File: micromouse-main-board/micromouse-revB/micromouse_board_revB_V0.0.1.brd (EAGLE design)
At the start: 128.4 x 85.5 mm, 110 parts, among them IC1 LM321MFX, J3 HTSS-103-XX-XX-D, J5 HTSS-103-XX-XX-D, J6 HTSS-102-XX-XX-D, U2 DRV8848PWPR, U3 ACS712ELCTR-20A-T, U6 MPU-6000, X1 RASPI_GPIO_B+#_PIN

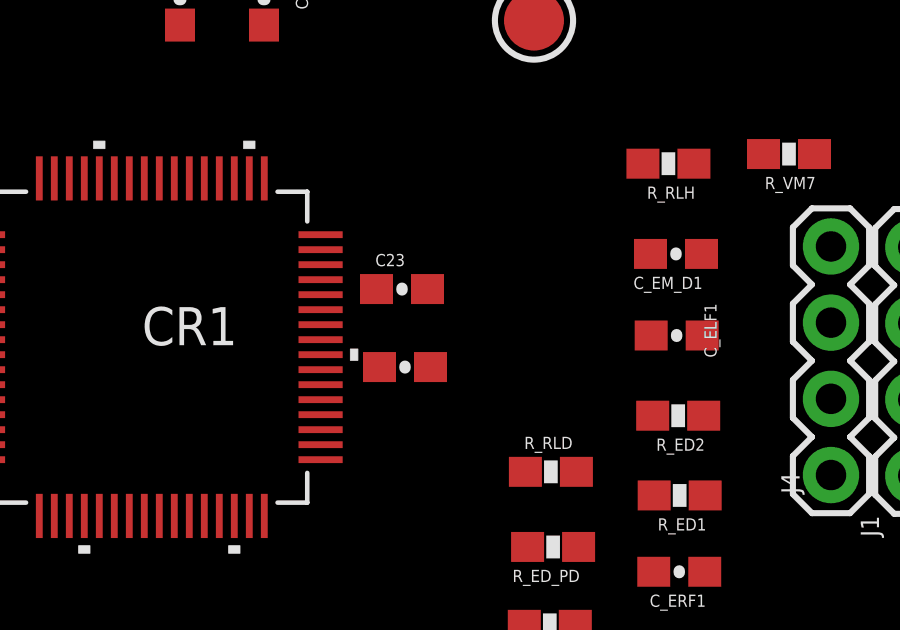
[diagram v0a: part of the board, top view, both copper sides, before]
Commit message: power reg. added placement done
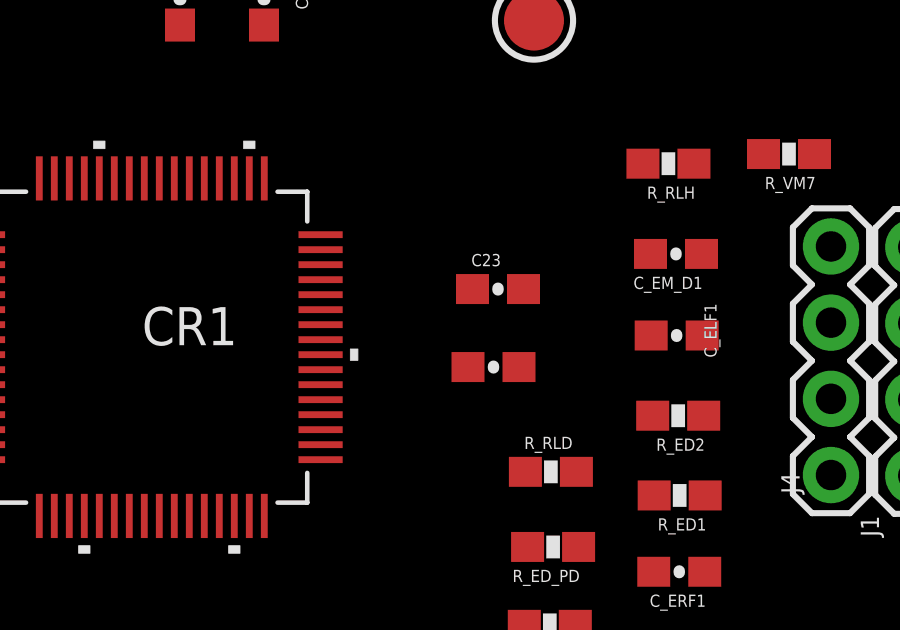
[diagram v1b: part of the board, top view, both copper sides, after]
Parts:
- moved C23 3.20 mm to (65.5, 49.1)
- moved C7 2.95 mm to (65.3, 46.5)
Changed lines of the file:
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@@
 <setting verticaltext="up"/>
 </settings>
-<grid distance="1.96850394" unitdist="mil" unit="mil" style="lines" multiple="1" display="yes" altdistance="1" altunitdist="mil" altunit="mil"/>
+<grid distance="5" unitdist="mm" unit="mm" style="lines" multiple="1" display="yes" altdistance="1" altunitdist="mil" altunit="mil"/>
 <layers>
 <layer number="1" name="Top" color="4" fill="1" visible="yes" active="yes"/>
@@
 <attribute name="VALUE" x="76.166" y="54.743" size="0.4064" layer="27" font="vector" rot="R180"/>
 </element>
-<element name="C7" library="micromouse-board-added-piconnector" library_urn="urn:adsk.eagle:library:14781578" package="0603-CAP" package3d_urn="urn:adsk.eagle:package:14781741/1" value="0.1uF" x="62.35" y="46.5" smashed="yes" rot="R180">
-<attribute name="NAME" x="63.239" y="45.738" size="0.4064" layer="26" font="vector" rot="MR180"/>
-<attribute name="VALUE" x="63.366" y="47.643" size="0.4064" layer="27" font="vector" rot="R180"/>
+<element name="C7" library="micromouse-board-added-piconnector" library_urn="urn:adsk.eagle:library:14781578" package="0603-CAP" package3d_urn="urn:adsk.eagle:package:14781741/1" value="0.1uF" x="65.3" y="46.5" smashed="yes" rot="R180">
+<attribute name="NAME" x="66.189" y="45.738" size="0.4064" layer="26" font="vector" rot="MR180"/>
+<attribute name="VALUE" x="66.316" y="47.643" size="0.4064" layer="27" font="vector" rot="R180"/>
 </element>
 <element name="C21" library="micromouse-board-added-piconnector" library_urn="urn:adsk.eagle:library:14781578" package="0603-CAP" package3d_urn="urn:adsk.eagle:package:14781741/1" value="4.7uF" x="61.15" y="64.35" smashed="yes" rot="R270">
@@
 <attribute name="VALUE" x="61.393" y="61.234" size="0.4064" layer="27" font="vector" rot="R90"/>
 </element>
-<element name="C23" library="micromouse-board-added-piconnector" library_urn="urn:adsk.eagle:library:14781578" package="0603-CAP" package3d_urn="urn:adsk.eagle:package:14781741/1" value="4.7uF" x="62.25" y="49.1" smashed="yes">
-<attribute name="NAME" x="61.361" y="49.862" size="0.4064" layer="25" font="vector"/>
-<attribute name="VALUE" x="61.234" y="47.957" size="0.4064" layer="27" font="vector"/>
+<element name="C23" library="micromouse-board-added-piconnector" library_urn="urn:adsk.eagle:library:14781578" package="0603-CAP" package3d_urn="urn:adsk.eagle:package:14781741/1" value="4.7uF" x="65.45" y="49.1" smashed="yes">
+<attribute name="NAME" x="64.561" y="49.862" size="0.4064" layer="25" font="vector"/>
+<attribute name="VALUE" x="64.434" y="47.957" size="0.4064" layer="27" font="vector"/>
 </element>
 <element name="JP1" library="micromouse-board-added-piconnector" library_urn="urn:adsk.eagle:library:14781578" package="MOLEX-1X2" package3d_urn="urn:adsk.eagle:package:14781763/1" value="" x="41.35" y="33.9" smashed="yes" rot="R90"/>
@@
 <wire x1="61.2" y1="61" x2="61.15" y2="65.2" width="0" layer="19" extent="1-1"/>
 <wire x1="59.5361" y1="50.413" x2="61.2" y2="61" width="0" layer="19" extent="1-1"/>
-<wire x1="61.4" y1="49.1" x2="59.5361" y2="50.413" width="0" layer="19" extent="1-16"/>
-<wire x1="61.5" y1="46.5" x2="61.4" y2="49.1" width="0" layer="19" extent="16-16"/>
-<wire x1="76.55" y1="42.9" x2="61.5" y2="46.5" width="0" layer="19" extent="16-16"/>
-<wire x1="79.293" y1="42.877" x2="61.4" y2="49.1" width="0" layer="19" extent="16-16"/>
+<wire x1="64.6" y1="49.1" x2="59.5361" y2="50.413" width="0" layer="19" extent="1-16"/>
+<wire x1="64.45" y1="46.5" x2="64.6" y2="49.1" width="0" layer="19" extent="16-16"/>
+<wire x1="76.55" y1="42.9" x2="64.45" y2="46.5" width="0" layer="19" extent="16-16"/>
+<wire x1="79.293" y1="42.877" x2="64.6" y2="49.1" width="0" layer="19" extent="16-16"/>
 <wire x1="57.16" y1="41.5369" x2="76.55" y2="42.9" width="0" layer="19" extent="1-1"/>
 <wire x1="50.66" y1="41.5369" x2="57.16" y2="41.5369" width="0" layer="19" extent="1-1"/>
@@
 <wire x1="61.2" y1="59.3" x2="61.15" y2="63.5" width="0" layer="19" extent="1-1"/>
 <wire x1="59.5361" y1="50.913" x2="61.2" y2="59.3" width="0" layer="19" extent="1-1"/>
-<wire x1="63.1" y1="49.1" x2="59.5361" y2="50.913" width="0" layer="19" extent="1-16"/>
-<wire x1="63.2" y1="46.5" x2="63.1" y2="49.1" width="0" layer="19" extent="16-16"/>
-<wire x1="76.55" y1="45.44" x2="63.2" y2="46.5" width="0" layer="19" extent="16-16"/>
+<wire x1="66.3" y1="49.1" x2="59.5361" y2="50.913" width="0" layer="19" extent="1-16"/>
+<wire x1="66.15" y1="46.5" x2="66.3" y2="49.1" width="0" layer="19" extent="16-16"/>
+<wire x1="76.55" y1="45.44" x2="66.15" y2="46.5" width="0" layer="19" extent="16-16"/>
 <wire x1="79.293" y1="50.497" x2="76.55" y2="45.44" width="0" layer="19" extent="1-1"/>
-<wire x1="57.66" y1="41.5369" x2="63.2" y2="46.5" width="0" layer="19" extent="1-16"/>
+<wire x1="57.66" y1="41.5369" x2="66.15" y2="46.5" width="0" layer="19" extent="1-16"/>
 <wire x1="51.16" y1="41.5369" x2="57.66" y2="41.5369" width="0" layer="19" extent="1-1"/>
 <wire x1="48.2839" y1="44.913" x2="51.16" y2="41.5369" width="0" layer="19" extent="1-1"/>
